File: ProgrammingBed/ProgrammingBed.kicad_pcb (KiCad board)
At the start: 2 copper layers, 30 x 30 mm, 8 parts, among them J1 Conn_01x06, J2 Conn_01x01, J3 Conn_01x01, J4 Conn_01x01, J5 Conn_01x01, J6 Conn_01x01

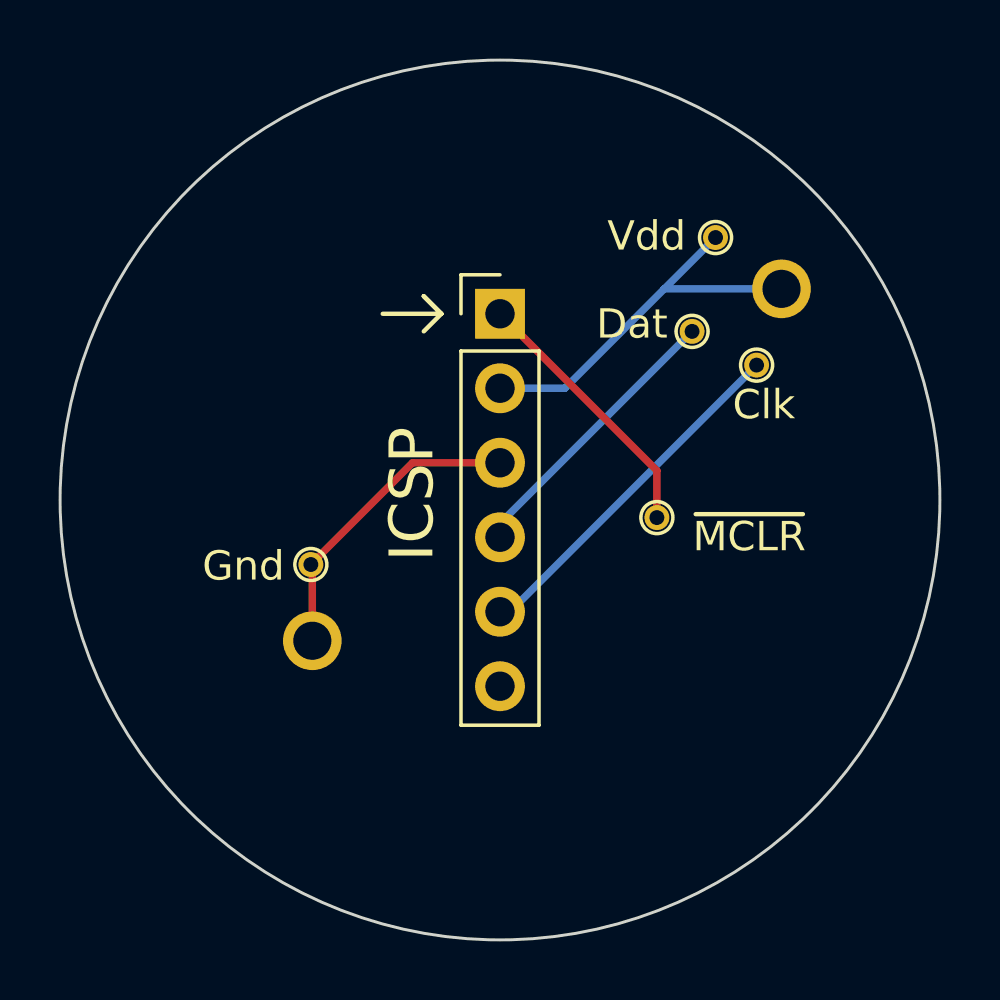
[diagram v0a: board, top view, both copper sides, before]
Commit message: Added BOM; added programming bed rev1 layout
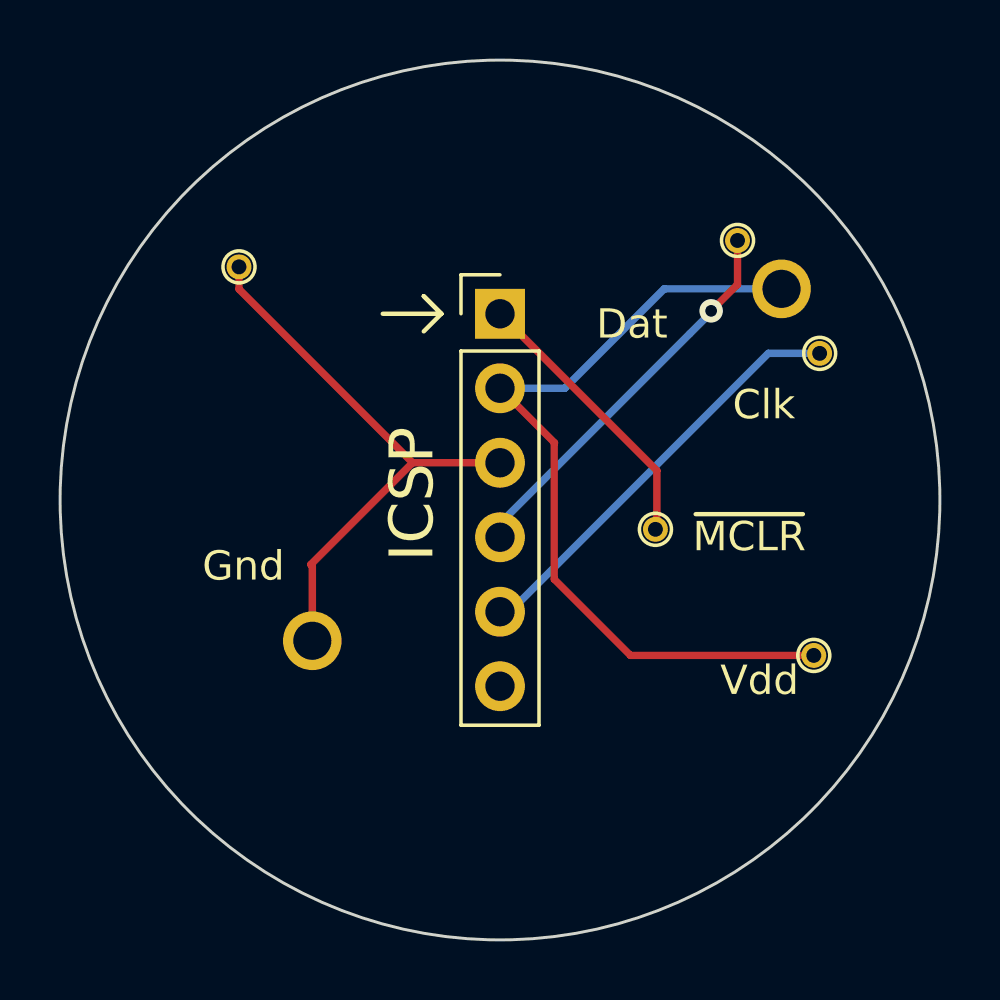
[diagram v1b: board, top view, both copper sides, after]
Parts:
- moved J3 14.6 mm to (10.7, 5.30)
- moved J4 10.4 mm to (-8.90, -7.95)
- moved J5 3.47 mm to (8.10, -8.85)
- moved J6 2.19 mm to (10.9, -5.00)
- moved J2 0.40 mm to (5.30, 1.00)
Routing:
- net Net-(H1-Pad1): track 13.5 -> 28.2 mm
- net Net-(H2-Pad1): track 10.5 -> 19.6 mm
- net Net-(J1-Pad4): track 9.73 -> 13.5 mm, vias 0 -> 1
- net Net-(J1-Pad5): track 12.2 -> 14.5 mm
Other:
- board text added: "Lightup Note Detector Programming Bed 03-20-2023, Rev1 Matt Dion"
- board text removed: "Lightup Note Detector Programming Bed 2-19-2023 Matthew Dion"
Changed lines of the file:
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@@
       (outputformat 1)
       (mirror false)
-      (drillshape 1)
+      (drillshape 0)
       (scaleselection 1)
-      (outputdirectory "")
+      (outputdirectory "production/Rev1/")
     )
   )
   (net 0 "")
   (net 1 "Net-(J1-Pad1)")
-  (net 2 "Net-(J1-Pad2)")
-  (net 3 "Net-(J1-Pad3)")
+  (net 2 "Net-(H1-Pad1)")
+  (net 3 "Net-(H2-Pad1)")
   (net 4 "Net-(J1-Pad4)")
   (net 5 "Net-(J1-Pad5)")
@@
     (fp_circle (center 0 0) (end 1 0) (layer "F.CrtYd") (width 0.05) (fill none))
     (pad "1" thru_hole circle (at 0 0) (size 2 2) (drill 1.3) (layers *.Cu *.Mask)
-      (net 3 "Net-(J1-Pad3)") (pinfunction "1") (pintype "input"))
+      (net 3 "Net-(H2-Pad1)") (pinfunction "1") (pintype "input"))
     (model "${KICAD6_3DMODEL_DIR}/Connector_PinHeader_1.27mm.3dshapes/PinHeader_1x01_P1.27mm_Vertical.wrl"
       (offset (xyz 0 0 0))
@@
       (net 1 "Net-(J1-Pad1)") (pinfunction "Pin_1") (pintype "passive"))
     (pad "2" thru_hole oval (at 0 2.54) (size 1.7 1.7) (drill 1) (layers *.Cu *.Mask)
-      (net 2 "Net-(J1-Pad2)") (pinfunction "Pin_2") (pintype "passive"))
+      (net 2 "Net-(H1-Pad1)") (pinfunction "Pin_2") (pintype "passive"))
     (pad "3" thru_hole oval (at 0 5.08) (size 1.7 1.7) (drill 1) (layers *.Cu *.Mask)
-      (net 3 "Net-(J1-Pad3)") (pinfunction "Pin_3") (pintype "passive"))
+      (net 3 "Net-(H2-Pad1)") (pinfunction "Pin_3") (pintype "passive"))
     (pad "4" thru_hole oval (at 0 7.62) (size 1.7 1.7) (drill 1) (layers *.Cu *.Mask)
       (net 4 "Net-(J1-Pad4)") (pinfunction "Pin_4") (pintype "passive"))
@@
     (fp_circle (center 0 0) (end 1 0) (layer "F.CrtYd") (width 0.05) (fill none))
     (pad "1" thru_hole circle (at 0 0) (size 2 2) (drill 1.3) (layers *.Cu *.Mask)
-      (net 2 "Net-(J1-Pad2)") (pinfunction "1") (pintype "input"))
+      (net 2 "Net-(H1-Pad1)") (pinfunction "1") (pintype "input"))
     (model "${KICAD6_3DMODEL_DIR}/Connector_PinHeader_1.27mm.3dshapes/PinHeader_1x01_P1.27mm_Vertical.wrl"
       (offset (xyz 0 0 0))
@@
   )
   (footprint "user:PogoPin" (layer "F.Cu")
-    (at 6.55 -5.75)
+    (at 8.1 -8.85)
     (descr "Mill-Max 0985-1-15-20-71-14-11-0")
     (tags "Through hole pogo pin")
@@
   )
   (footprint "user:PogoPin" (layer "F.Cu")
-    (at 5.35 0.6)
+    (at 5.3 1)
     (descr "Mill-Max 0985-1-15-20-71-14-11-0")
     (tags "Through hole pogo pin")
@@
   )
   (footprint "user:PogoPin" (layer "F.Cu")
-    (at 7.35 -8.95)
+    (at 10.7 5.3)
     (descr "Mill-Max 0985-1-15-20-71-14-11-0")
     (tags "Through hole pogo pin")
@@
     (fp_circle (center 0 0) (end 0.5461 0) (layer "F.CrtYd") (width 0.12) (fill none))
     (pad "1" thru_hole circle (at 0 0) (size 0.85 0.85) (drill 0.508) (layers *.Cu *.Mask)
-      (net 2 "Net-(J1-Pad2)") (pinfunction "Pin_1") (pintype "passive"))
-    (model "${KICAD6_3DMODEL_DIR}/Connector_PinHeader_1.00mm.3dshapes/PinHeader_1x01_P1.00mm_Vertical.wrl"
-      (offset (xyz 0 0 0))
-      (scale (xyz 1 1 1))
-      (rotate (xyz 0 0 0))
-    )
-  )
-  (footprint "user:PogoPin" (layer "F.Cu")
-    (at -6.45 2.2)
+      (net 2 "Net-(H1-Pad1)") (pinfunction "Pin_1") (pintype "passive"))
+    (model "${KICAD6_3DMODEL_DIR}/Connector_PinHeader_1.00mm.3dshapes/PinHeader_1x01_P1.00mm_Vertical.wrl"
+      (offset (xyz 0 0 0))
+      (scale (xyz 1 1 1))
+      (rotate (xyz 0 0 0))
+    )
+  )
+  (footprint "user:PogoPin" (layer "F.Cu")
+    (at -8.9 -7.95)
     (descr "Mill-Max 0985-1-15-20-71-14-11-0")
     (tags "Through hole pogo pin")
@@
     (fp_circle (center 0 0) (end 0.5461 0) (layer "F.CrtYd") (width 0.12) (fill none))
     (pad "1" thru_hole circle (at 0 0) (size 0.85 0.85) (drill 0.508) (layers *.Cu *.Mask)
-      (net 3 "Net-(J1-Pad3)") (pinfunction "Pin_1") (pintype "passive"))
-    (model "${KICAD6_3DMODEL_DIR}/Connector_PinHeader_1.00mm.3dshapes/PinHeader_1x01_P1.00mm_Vertical.wrl"
-      (offset (xyz 0 0 0))
-      (scale (xyz 1 1 1))
-      (rotate (xyz 0 0 0))
-    )
-  )
-  (footprint "user:PogoPin" (layer "F.Cu")
-    (at 8.75 -4.6)
+      (net 3 "Net-(H2-Pad1)") (pinfunction "Pin_1") (pintype "passive"))
+    (model "${KICAD6_3DMODEL_DIR}/Connector_PinHeader_1.00mm.3dshapes/PinHeader_1x01_P1.00mm_Vertical.wrl"
+      (offset (xyz 0 0 0))
+      (scale (xyz 1 1 1))
+      (rotate (xyz 0 0 0))
+    )
+  )
+  (footprint "user:PogoPin" (layer "F.Cu")
+    (at 10.9 -5)
     (descr "Mill-Max 0985-1-15-20-71-14-11-0")
     (tags "Through hole pogo pin")
@@
   (gr_circle (center 0 0) (end 12.7 0) (layer "Dwgs.User") (width 0.2) (fill none))
   (gr_circle (center 0 0) (end 15 0) (layer "Edge.Cuts") (width 0.1) (fill none))
-  (gr_text "Lightup Note Detector\nProgramming Bed\n2-19-2023\nMatthew Dion" (at -5.8 -3.6 270) (layer "B.SilkS")
+  (gr_text "Lightup Note Detector\nProgramming Bed\n03-20-2023, Rev1\nMatt Dion" (at -5.8 -3.6 270) (layer "B.SilkS")
     (effects (font (size 0.75 0.75) (thickness 0.15)) (justify mirror))
   )
@@
     (effects (font (size 1 1) (thickness 0.15)))
   )
-  (gr_text "Vdd" (at 5 -9) (layer "F.SilkS")
+  (gr_text "Vdd" (at 8.85 6.15) (layer "F.SilkS")
     (effects (font (size 1 1) (thickness 0.15)))
   )
@@
   (segment (start 5.35 0.6) (end 5.35 -1) (width 0.254) (layer "F.Cu") (net 1))
   (segment (start 5.35 -1) (end 0 -6.35) (width 0.254) (layer "F.Cu") (net 1))
+  (segment (start 1.85 -1.94) (end 1.86 -1.95) (width 0.25) (layer "F.Cu") (net 2))
+  (segment (start 1.85 2.7) (end 1.85 -1.94) (width 0.25) (layer "F.Cu") (net 2))
+  (segment (start 4.45 5.3) (end 1.85 2.7) (width 0.25) (layer "F.Cu") (net 2))
+  (segment (start 1.86 -1.95) (end 0 -3.81) (width 0.25) (layer "F.Cu") (net 2))
+  (segment (start 10.7 5.3) (end 4.45 5.3) (width 0.25) (layer "F.Cu") (net 2))
   (segment (start 0 -3.81) (end 2.21 -3.81) (width 0.254) (layer "B.Cu") (net 2))
   (segment (start 2.21 -3.81) (end 5.6 -7.2) (width 0.254) (layer "B.Cu") (net 2))
   (segment (start 9.6 -7.2) (end 5.6 -7.2) (width 0.254) (layer "B.Cu") (net 2))
-  (segment (start 5.6 -7.2) (end 7.35 -8.95) (width 0.254) (layer "B.Cu") (net 2))
   (segment (start -6.4 2.25) (end -6.45 2.2) (width 0.254) (layer "F.Cu") (net 3))
   (segment (start -2.98 -1.27) (end -6.45 2.2) (width 0.254) (layer "F.Cu") (net 3))
   (segment (start -6.4 4.8) (end -6.4 2.25) (width 0.254) (layer "F.Cu") (net 3))
+  (segment (start -8.9 -7.19) (end -2.98 -1.27) (width 0.25) (layer "F.Cu") (net 3))
   (segment (start 0 -1.27) (end -2.98 -1.27) (width 0.254) (layer "F.Cu") (net 3))
-  (segment (start 6.55 -5.75) (end 0 0.8) (width 0.254) (layer "B.Cu") (net 4))
+  (segment (start -8.9 -7.95) (end -8.9 -7.19) (width 0.25) (layer "F.Cu") (net 3))
+  (segment (start 7.2 -6.45) (end 8.1 -7.35) (width 0.254) (layer "F.Cu") (net 4))
+  (segment (start 8.1 -7.35) (end 8.1 -8.85) (width 0.254) (layer "F.Cu") (net 4))
+  (via (at 7.2 -6.45) (size 0.8) (drill 0.4) (layers "F.Cu" "B.Cu") (net 4))
+  (segment (start 6.475 -5.675) (end 0 0.8) (width 0.254) (layer "B.Cu") (net 4))
   (segment (start 0 0.8) (end 0 1.27) (width 0.254) (layer "B.Cu") (net 4))
+  (segment (start 7.2 -6.4) (end 7.2 -6.45) (width 0.254) (layer "B.Cu") (net 4))
+  (segment (start 6.475 -5.675) (end 7.2 -6.4) (width 0.254) (layer "B.Cu") (net 4))
   (segment (start 0.34 3.81) (end 0 3.81) (width 0.254) (layer "B.Cu") (net 5))
-  (segment (start 8.75 -4.6) (end 0.34 3.81) (width 0.254) (layer "B.Cu") (net 5))
+  (segment (start 9.15 -5) (end 0.34 3.81) (width 0.254) (layer "B.Cu") (net 5))
+  (segment (start 10.9 -5) (end 9.15 -5) (width 0.254) (layer "B.Cu") (net 5))
 )

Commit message: Changelog: combined midscale references; added reverse voltage protection; moved ~MCLR programming pad to board perimeter; increased min drill/pad size
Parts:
- moved J2 7.63 mm to (9.11, 7.61)
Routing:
- net Net-(J1-Pad1): track 9.17 -> 18.0 mm, vias 0 -> 1
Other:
- board text added: "Lightup Note Detector Programming Bed 11-24-2024, Rev2 Matt Dion"
- board text removed: "Lightup Note Detector Programming Bed 03-20-2023, Rev1 Matt Dion"
